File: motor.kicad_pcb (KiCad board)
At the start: 2 copper layers, 100 x 100 mm, 74 parts, among them J1 Gates_B, J2 PWM_B, J3 I2C, J41 Jump_ID_A, J43 ATX_power, J46 Fan_vol_sel, J48 Power_male, J49 Power_female, J50 Power_signal_male, J51 Power_signal_female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

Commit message: PCB: Update
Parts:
- D61, D63: footprint Diode_THT:D_5W_P10.16mm_Horizontal -> Diode_THT:D_5W_P12.70mm_Horizontal
- J3, J61: footprint TerminalBlock_4Ucon:TerminalBlock_4Ucon_1x02_P3.50mm_Vertical -> TerminalBlock:TerminalBlock_Altech_AK300-2_P5.00mm
- R44: footprint Resistor_THT:R_Axial_DIN0309_L9.0mm_D3.2mm_P25.40mm_Horizontal -> Resistor_THT:R_Axial_Power_L20.0mm_W6.4mm_P22.40mm
- R63: footprint Resistor_THT:R_Axial_DIN0309_L9.0mm_D3.2mm_P2.54mm_Vertical -> Resistor_THT:R_Axial_DIN0309_L9.0mm_D3.2mm_P12.70mm_Horizontal
- moved R63 10.2 mm to (85.1, 83.8)
- moved D63 3.17 mm to (101.0, 78.7)
- moved J61 2.62 mm to (97.2, 94.0)
- moved J3 1.80 mm to (132.1, 146.1)
- moved Y1 0.64 mm to (93.9, 131.4)
- moved D61 0.63 mm to (95.9, 78.7)
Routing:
- net +12V: track 104.1 -> 225.0 mm, vias 0 -> 4
- net /Gate_POS_P: track 2.54 -> 118.0 mm, vias 0 -> 5
- net /~PS_ON~: track 0.00 -> 114.0 mm, vias 0 -> 4
- net /Gate_POS_N: track 2.54 -> 74.4 mm, vias 0 -> 4
- net GND: track 71.9 -> 138.3 mm, vias 0 -> 2
- net +5VD: track 213.3 -> 258.7 mm
- net /PWR_OK: track 0.00 -> 38.7 mm
- net -12V: track 124.7 -> 129.3 mm
- net /SCL: track 22.9 -> 25.7 mm
- net Net-(D61-Pad1): track 7.62 -> 5.08 mm
- net /SDA: track 22.0 -> 23.8 mm
- net /Gate_B_NEG_N: track 28.5 -> 27.8 mm
- net /Gate_B_NEG_P: track 26.0 -> 25.2 mm
- net /Gate_B_POS_N: track 23.4 -> 22.7 mm
- net Net-(U1-Pad9): track 4.34 -> 3.68 mm
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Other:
- rule trace_min: 0.2 -> 0.25

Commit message: Do not connect PWR_OK to AVR
It is too far!  If you need it, connect it by your hand.
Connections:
- U1 pad 18: /PWR_OK -> (no net)
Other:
- rule trace_min: 0.25 -> 0.3
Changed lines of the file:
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@@
     (zone_clearance 0.508)
     (zone_45_only no)
-    (trace_min 0.25)
+    (trace_min 0.3)
     (segment_width 0.2)
     (edge_width 0.1)
@@
     (pad 4 thru_hole oval (at 0 7.62 270) (size 1.6 1.6) (drill 0.8) (layers *.Cu *.Mask)
       (net 17 /Gate_A_POS_N))
-    (pad 18 thru_hole oval (at 7.62 25.4 270) (size 1.6 1.6) (drill 0.8) (layers *.Cu *.Mask)
-      (net 24 /PWR_OK))
+    (pad 18 thru_hole oval (at 7.62 25.4 270) (size 1.6 1.6) (drill 0.8) (layers *.Cu *.Mask))
     (pad 5 thru_hole oval (at 0 10.16 270) (size 1.6 1.6) (drill 0.8) (layers *.Cu *.Mask)
       (net 18 /Gate_A_POS_P))

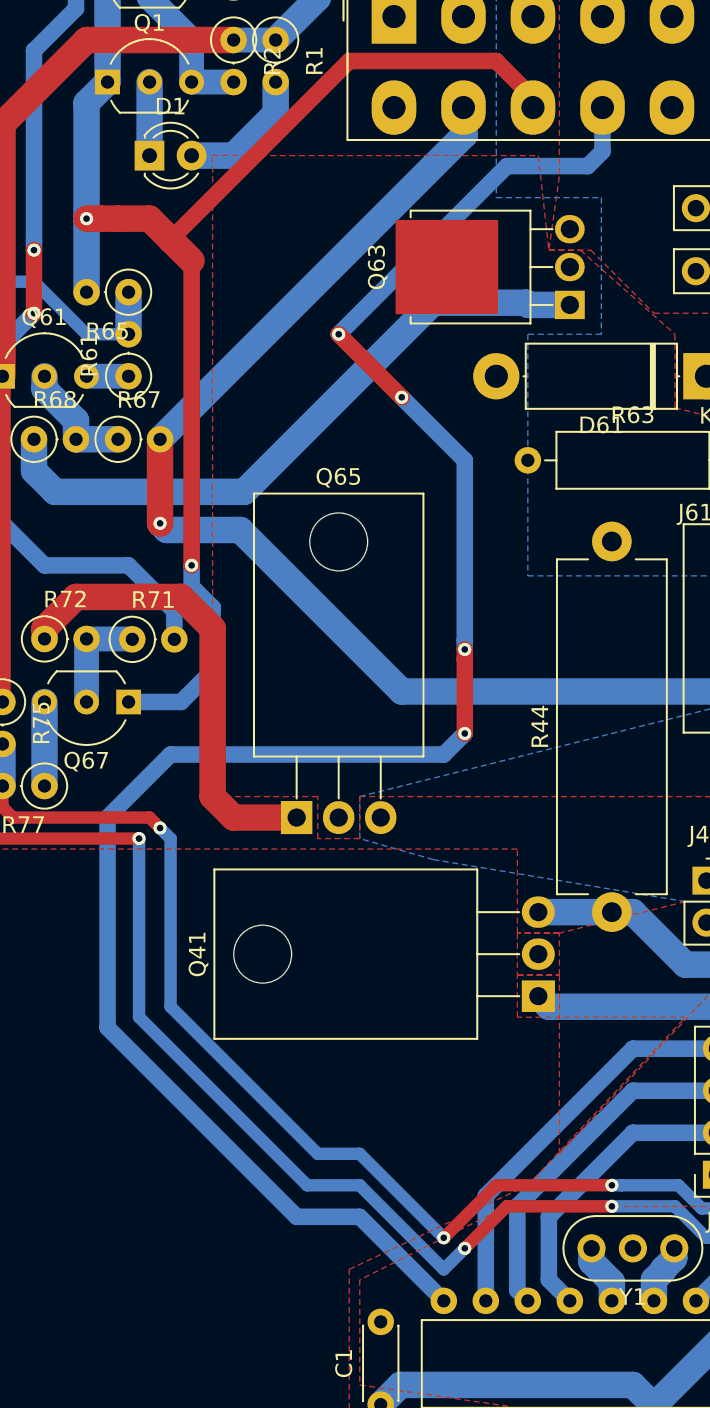
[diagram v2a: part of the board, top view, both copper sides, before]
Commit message: PCB: Add solder masks as heat sinks
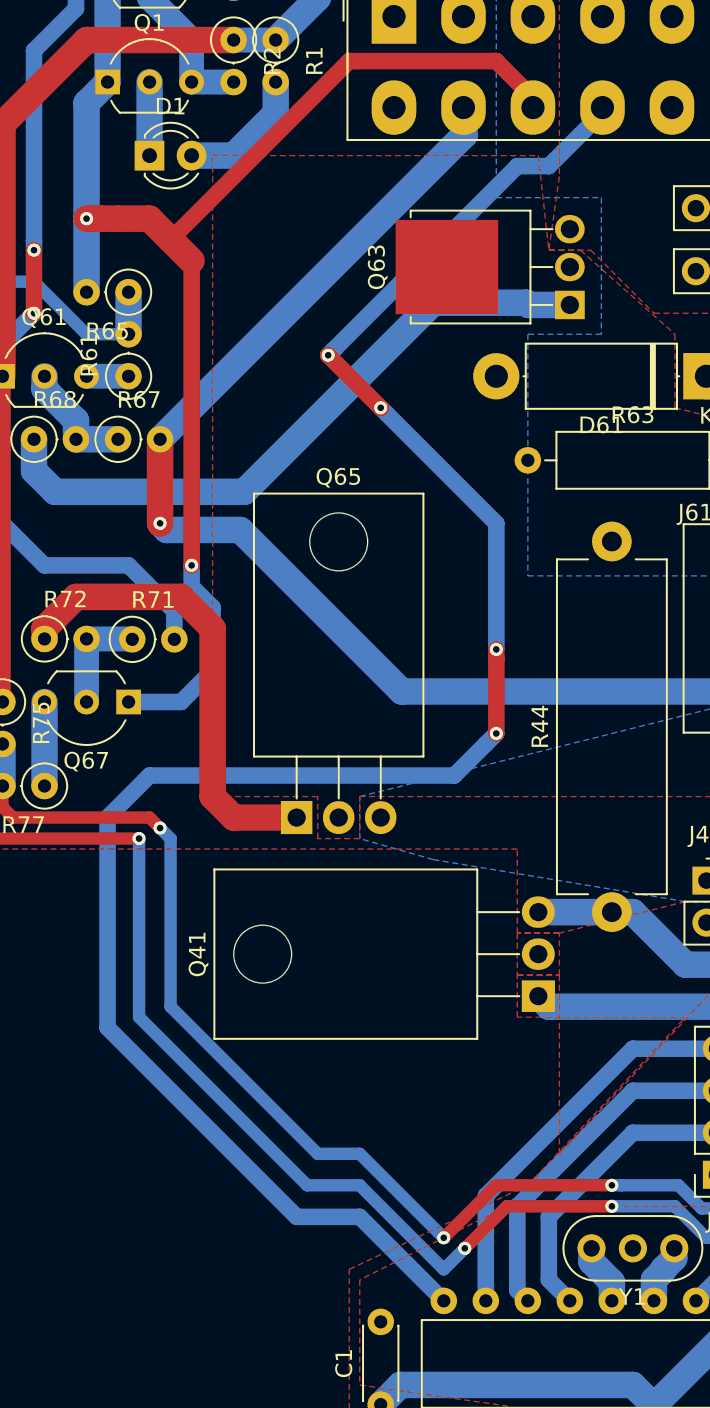
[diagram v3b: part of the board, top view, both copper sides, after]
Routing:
- net /~PS_ON~: track 114.0 -> 115.5 mm
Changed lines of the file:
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@@
     (thickness 1.6)
     (drawings 12)
-    (tracks 386)
+    (tracks 389)
     (zones 0)
     (modules 74)
@@
   (segment (start 146.05 83.04637) (end 143.75237 85.344) (width 1.6) (layer B.Cu) (net 25))
   (segment (start 146.05 81.915) (end 146.05 83.04637) (width 1.6) (layer B.Cu) (net 25))
-  (segment (start 89.6 65.15) (end 88.71 66.04) (width 1) (layer B.Cu) (net 26))
-  (segment (start 89.6 62.5) (end 89.6 65.15) (width 1) (layer B.Cu) (net 26))
-  (via (at 73.66 76.2) (size 0.8) (drill 0.4) (layers F.Cu B.Cu) (net 26))
-  (segment (start 83.82 66.04) (end 73.66 76.2) (width 1) (layer B.Cu) (net 26))
-  (segment (start 88.71 66.04) (end 83.82 66.04) (width 1) (layer B.Cu) (net 26))
-  (via (at 77.47 80.01) (size 0.8) (drill 0.4) (layers F.Cu B.Cu) (net 26))
-  (segment (start 73.66 76.2) (end 77.47 80.01) (width 1) (layer F.Cu) (net 26))
-  (segment (start 81.28 94.684315) (end 81.28 95.25) (width 1) (layer B.Cu) (net 26))
-  (segment (start 77.47 80.01) (end 81.28 83.82) (width 1) (layer B.Cu) (net 26))
-  (segment (start 81.28 83.82) (end 81.28 94.684315) (width 1) (layer B.Cu) (net 26))
-  (via (at 81.28 95.25) (size 0.8) (drill 0.4) (layers F.Cu B.Cu) (net 26))
-  (segment (start 81.28 95.815685) (end 81.28 100.33) (width 1) (layer F.Cu) (net 26))
-  (segment (start 81.28 95.25) (end 81.28 95.815685) (width 1) (layer F.Cu) (net 26))
-  (via (at 81.28 100.33) (size 0.8) (drill 0.4) (layers F.Cu B.Cu) (net 26))
-  (segment (start 74.93 129.54) (end 80.01 134.62) (width 1) (layer B.Cu) (net 26))
-  (segment (start 59.69 118.11) (end 71.12 129.54) (width 1) (layer B.Cu) (net 26))
-  (segment (start 59.69 105.41) (end 59.69 118.11) (width 1) (layer B.Cu) (net 26))
-  (segment (start 63.5 101.6) (end 59.69 105.41) (width 1) (layer B.Cu) (net 26))
-  (segment (start 71.12 129.54) (end 74.93 129.54) (width 1) (layer B.Cu) (net 26))
-  (segment (start 80.01 101.6) (end 63.5 101.6) (width 1) (layer B.Cu) (net 26))
-  (segment (start 81.28 100.33) (end 80.01 101.6) (width 1) (layer B.Cu) (net 26))
+  (segment (start 73.424999 77.070001) (end 73.025 77.47) (width 1) (layer B.Cu) (net 26))
+  (segment (start 84.455 66.04) (end 73.424999 77.070001) (width 1) (layer B.Cu) (net 26))
+  (segment (start 86.36 66.04) (end 84.455 66.04) (width 1) (layer B.Cu) (net 26))
+  (segment (start 89.6 62.8) (end 86.36 66.04) (width 1) (layer B.Cu) (net 26))
+  (segment (start 89.6 62.5) (end 89.6 62.8) (width 1) (layer B.Cu) (net 26))
+  (via (at 73.025 77.47) (size 0.8) (drill 0.4) (layers F.Cu B.Cu) (net 26))
+  (via (at 83.185 95.25) (size 0.8) (drill 0.4) (layers F.Cu B.Cu) (net 26))
+  (segment (start 83.185 95.815685) (end 83.185 100.33) (width 1) (layer F.Cu) (net 26))
+  (segment (start 83.185 95.25) (end 83.185 95.815685) (width 1) (layer F.Cu) (net 26))
+  (via (at 83.185 100.33) (size 0.8) (drill 0.4) (layers F.Cu B.Cu) (net 26))
+  (segment (start 80.645 102.87) (end 82.55 100.965) (width 1) (layer B.Cu) (net 26))
+  (segment (start 59.69 105.41) (end 62.23 102.87) (width 1) (layer B.Cu) (net 26))
+  (segment (start 71.12 129.54) (end 59.69 118.11) (width 1) (layer B.Cu) (net 26))
+  (segment (start 62.23 102.87) (end 80.645 102.87) (width 1) (layer B.Cu) (net 26))
+  (segment (start 74.93 129.54) (end 71.12 129.54) (width 1) (layer B.Cu) (net 26))
+  (segment (start 82.55 100.965) (end 83.185 100.33) (width 1) (layer B.Cu) (net 26))
+  (segment (start 59.69 118.11) (end 59.69 105.41) (width 1) (layer B.Cu) (net 26))
+  (segment (start 80.01 134.62) (end 74.93 129.54) (width 1) (layer B.Cu) (net 26))
+  (via (at 76.199984 80.645) (size 0.8) (drill 0.4) (layers F.Cu B.Cu) (net 26))
+  (segment (start 76.199984 80.644984) (end 76.199984 80.645) (width 1) (layer F.Cu) (net 26))
+  (segment (start 83.185 87.630016) (end 76.599983 81.044999) (width 1) (layer B.Cu) (net 26))
+  (segment (start 73.025 77.47) (end 76.199984 80.644984) (width 1) (layer F.Cu) (net 26))
+  (segment (start 83.185 95.25) (end 83.185 87.630016) (width 1) (layer B.Cu) (net 26))
+  (segment (start 76.599983 81.044999) (end 76.199984 80.645) (width 1) (layer B.Cu) (net 26))
   (segment (start 144.145 61.595) (end 145.415 62.865) (width 1.6) (layer B.Cu) (net 27))
   (segment (start 144.145 58.512919) (end 144.145 61.595) (width 1.6) (layer B.Cu) (net 27))
@@
     (polygon
       (pts
-        (xy 58.42 107.95) (xy 82.55 107.95) (xy 82.55 123.825) (xy 58.42 123.825)
+        (xy 52.07 107.95) (xy 83.185 107.95) (xy 83.185 126.365) (xy 52.07 143.51)
       )
     )
@@
       )
     )
+  )
+  (zone (net 0) (net_name "") (layer F.Mask) (hatch edge 0.508)
+    (priority 7)
+    (connect_pads yes (clearance 0.508))
+    (min_thickness 0.254)
+    (fill yes (arc_segments 16) (thermal_gap 0.508) (thermal_bridge_width 0.508) (smoothing fillet) (radius 1))
+    (polygon
+      (pts
+        (xy 85.09 76.2) (xy 81.28 76.2) (xy 81.28 81.915) (xy 83.185 81.915) (xy 83.185 93.345)
+        (xy 81.915 93.345) (xy 81.915 102.87) (xy 67.945 102.87) (xy 67.945 92.075) (xy 66.675 92.075)
+        (xy 66.675 76.835) (xy 71.755 76.835) (xy 71.755 81.915) (xy 77.47 81.915) (xy 77.47 76.2)
+        (xy 66.675 76.2) (xy 66.675 69.215) (xy 69.85 66.04) (xy 85.09 66.04)
+      )
+    )
+  )
+  (zone (net 0) (net_name "") (layer F.Mask) (hatch edge 0.508)
+    (priority 7)
+    (connect_pads yes (clearance 0.508))
+    (min_thickness 0.254)
+    (fill yes (arc_segments 16) (thermal_gap 0.508) (thermal_bridge_width 0.508) (smoothing fillet) (radius 1))
+    (polygon
+      (pts
+        (xy 73.66 132.08) (xy 73.66 149.225) (xy 58.42 149.225) (xy 58.42 143.51) (xy 52.07 143.51)
+        (xy 52.07 126.365) (xy 83.185 126.365)
+      )
+    )
+  )
+  (zone (net 0) (net_name "") (layer F.Mask) (hatch edge 0.508)
+    (priority 7)
+    (connect_pads yes (clearance 0.508))
+    (min_thickness 0.254)
+    (fill yes (arc_segments 16) (thermal_gap 0.508) (thermal_bridge_width 0.508) (smoothing fillet) (radius 1))
+    (polygon
+      (pts
+        (xy 116.84 71.755) (xy 116.84 81.915) (xy 114.3 81.915) (xy 114.3 99.06) (xy 106.045 99.06)
+        (xy 106.045 111.76) (xy 133.985 111.76) (xy 133.985 93.345) (xy 132.08 92.075) (xy 132.08 71.755)
+      )
+    )
+  )
+  (zone (net 0) (net_name "") (layer F.Mask) (hatch edge 0.508)
+    (connect_pads yes (clearance 0.508))
+    (min_thickness 0.254)
+    (fill yes (arc_segments 16) (thermal_gap 0.508) (thermal_bridge_width 0.508) (smoothing fillet) (radius 1))
+    (polygon
+      (pts
+        (xy 66.675 74.295) (xy 66.675 79.375) (xy 71.755 79.375) (xy 71.755 74.295)
+      )
+    )

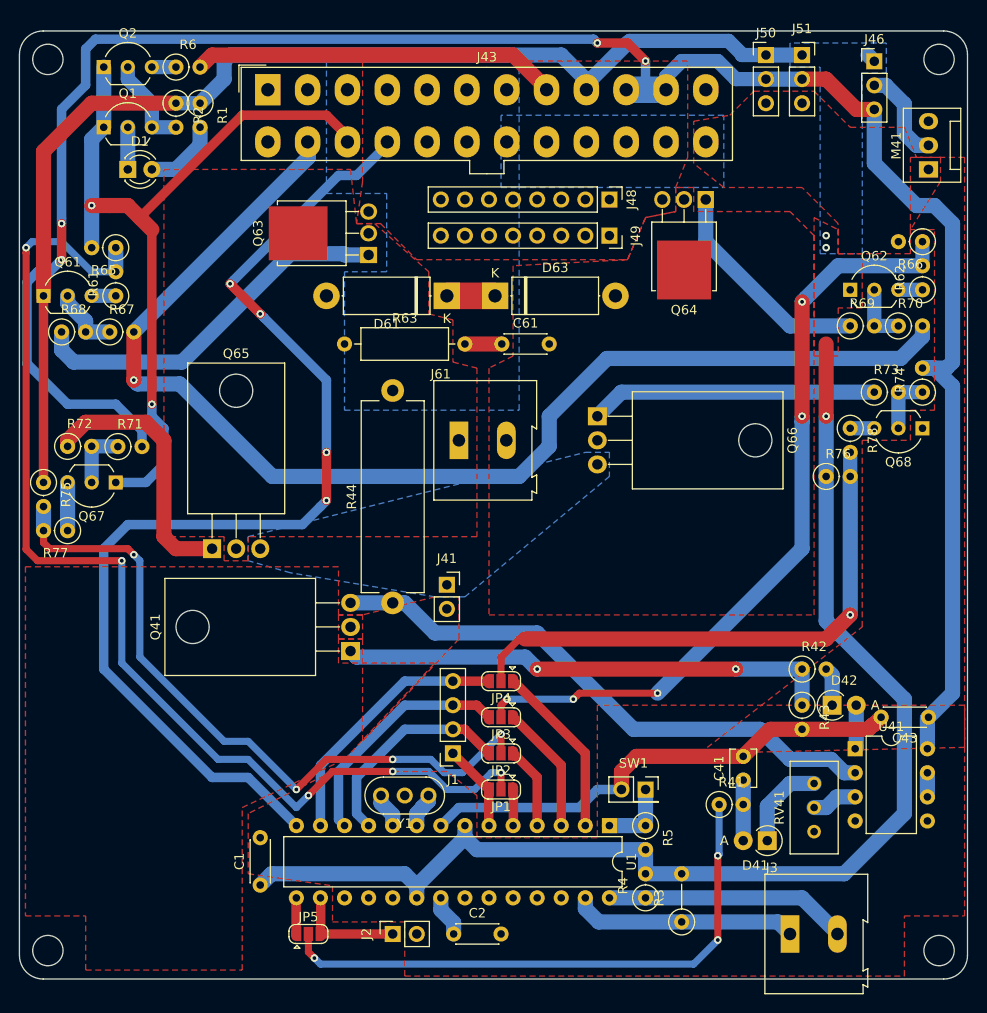
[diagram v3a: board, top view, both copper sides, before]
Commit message: PCB: Add vias to filled zones
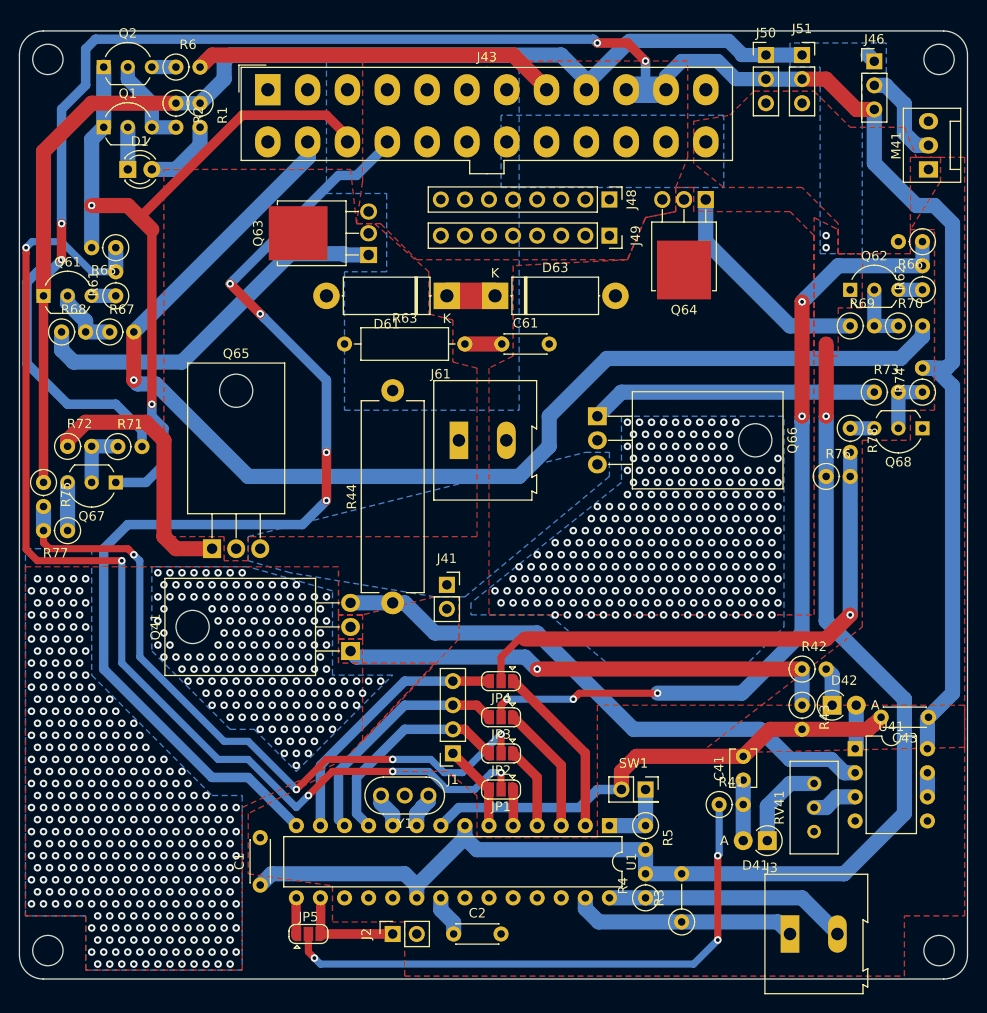
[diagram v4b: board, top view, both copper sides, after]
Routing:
- net /Gate_NEG_P: track 82.7 -> 87.9 mm
- net Net-(Q41-Pad1): vias 2 -> 1
- net Net-(J41-Pad2): vias 0 -> 544
- net /Driver/Motor_~A~: vias 0 -> 279
- added copper zone on B.Cu, net /Driver/Motor_~A~
- added copper zone on B.Cu, net Net-(J41-Pad2)

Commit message: PCB: Add a copyright text
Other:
- board text added: "Motor driver v.0.0.0 for the new planetarium projector ©2018 Tsukuba Univ. Astronomy Club Designed by Y. Sugizaki (45th)"
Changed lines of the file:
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@@
   (general
     (thickness 1.6)
-    (drawings 12)
+    (drawings 13)
     (tracks 1211)
     (zones 0)
@@
     (descr "TO-92 leads in-line, wide, drill 0.75mm (see NXP sot054_po.pdf)")
     (tags "to-92 sc-43 sc-43a sot54 PA33 transistor")
-    (fp_text reference Q68 (at 2.54 -3.56 180) (layer F.SilkS)
+    (fp_text reference Q68 (at -1.905 -1.905 180) (layer F.SilkS)
       (effects (font (size 1 1) (thickness 0.15)))
     )
@@
     )
   )
+  (gr_text "Motor driver v.0.0.0\nfor the new planetarium projector\n©2018 Tsukuba Univ. Astronomy Club\nDesigned by Y. Sugizaki (45th)" (at 144.145 108.585 90) (layer F.Mask)
+    (effects (font (size 1.4 0.9) (thickness 0.15)))
+  )
   (dimension 50 (width 0.3) (layer F.Fab)
